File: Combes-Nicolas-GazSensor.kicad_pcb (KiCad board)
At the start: 2 copper layers, 68.6 x 53.3 mm, 8 parts, among them P1 Power, P2 Analog, P3 Digital, P4 Digital, P5 CONN_01X01, P6 CONN_01X01, P7 CONN_01X01, P8 CONN_01X01

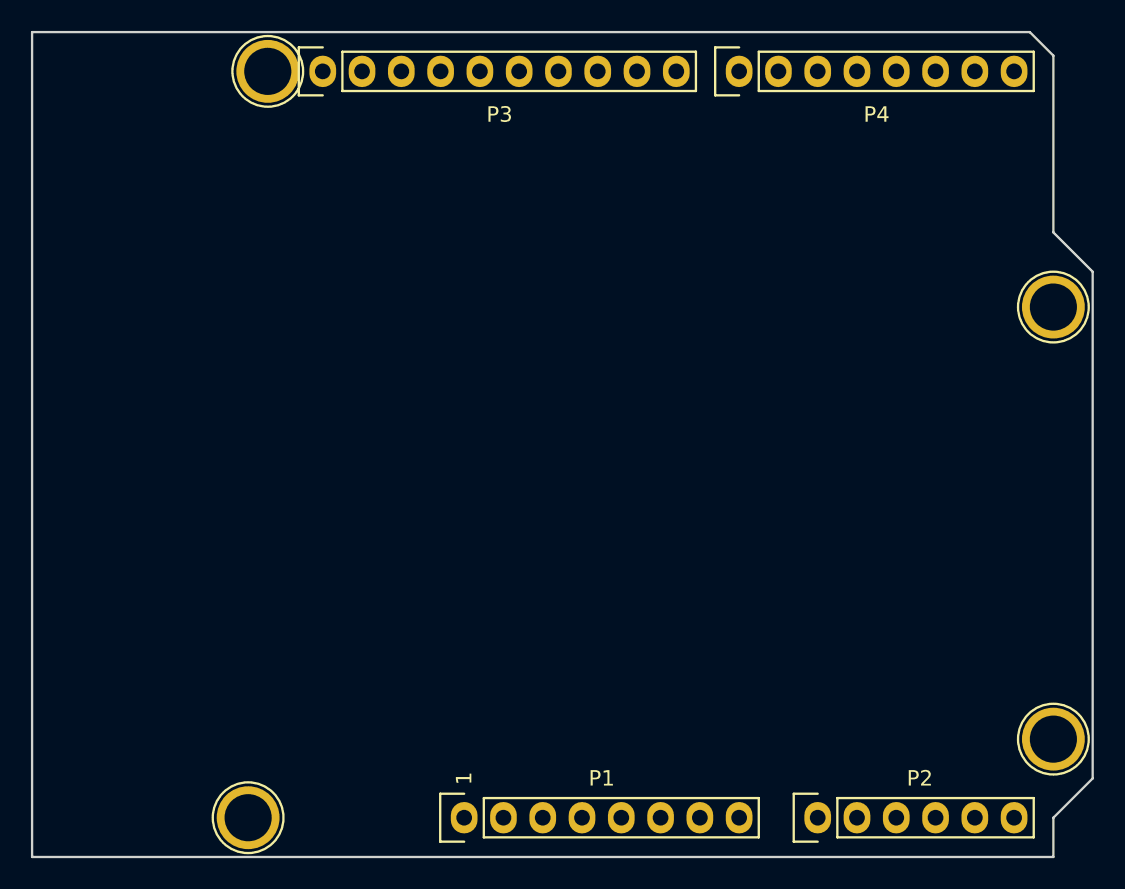
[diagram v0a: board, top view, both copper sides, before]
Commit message: Shield Capteur
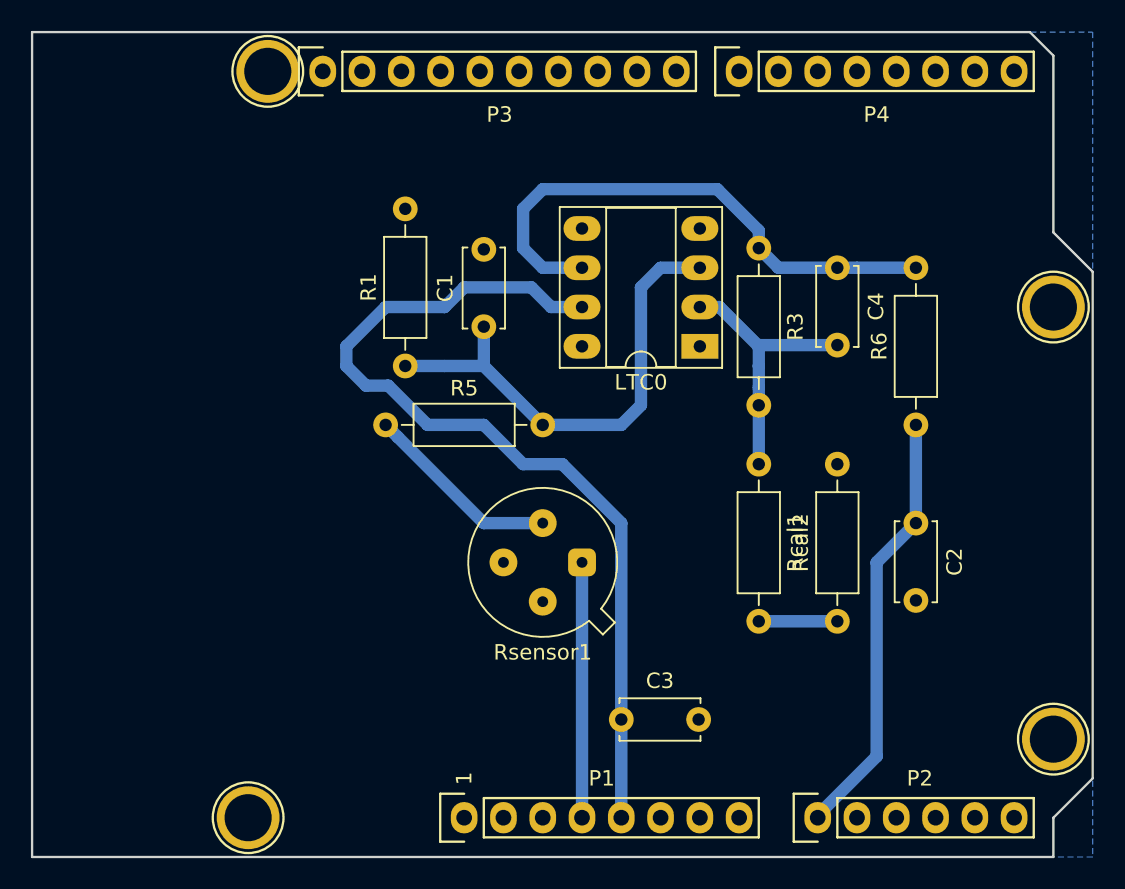
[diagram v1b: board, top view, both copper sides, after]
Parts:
- added C1: 100n, Capacitor_THT:C_Disc_D5.0mm_W2.5mm_P5.00mm, F.Cu at (140.2, 92.1)
- added C2: 100n, Capacitor_THT:C_Disc_D5.0mm_W2.5mm_P5.00mm, F.Cu at (168.1, 104.8)
- added C3: 100n, Capacitor_THT:C_Disc_D5.0mm_W2.5mm_P5.00mm, F.Cu at (149.1, 117.5)
- added C4: 1u, Capacitor_THT:C_Disc_D5.0mm_W2.5mm_P5.00mm, F.Cu at (163.1, 88.3)
- added LTC0: LTC1050, Package_DIP:DIP-8_W7.62mm_Socket_LongPads, F.Cu at (154.2, 93.3)
- added R1: 100k, Resistor_THT:R_Axial_DIN0207_L6.3mm_D2.5mm_P10.16mm_Horizontal, F.Cu at (135.1, 94.6)
- added R3: 100k, Resistor_THT:R_Axial_DIN0207_L6.3mm_D2.5mm_P10.16mm_Horizontal, F.Cu at (158.0, 87.0)
- added R5: 10k, Resistor_THT:R_Axial_DIN0207_L6.3mm_D2.5mm_P10.16mm_Horizontal, F.Cu at (133.9, 98.4)
- added R6: 1k, Resistor_THT:R_Axial_DIN0207_L6.3mm_D2.5mm_P10.16mm_Horizontal, F.Cu at (168.1, 98.4)
- added Rcal1: 1k, Resistor_THT:R_Axial_DIN0207_L6.3mm_D2.5mm_P10.16mm_Horizontal, F.Cu at (158.0, 101.0)
- added Rcal2: 220, Resistor_THT:R_Axial_DIN0207_L6.3mm_D2.5mm_P10.16mm_Horizontal, F.Cu at (163.1, 111.1)
- added Rsensor1: 10k<...<1G, MesEmpreintes:TO-5-4, F.Cu at (146.6, 107.3)
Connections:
- P1 pad 1: Net-(P1-Pad1) -> (no net)
- P1 pad 2: /IOREF -> (no net)
- P1 pad 3: /Reset -> (no net)
- P1 pad 8: /Vin -> (no net)
- P2 pad 1: /A0 -> A0
- P2 pad 2: /A1 -> (no net)
- P2 pad 3: /A2 -> (no net)
- P2 pad 4: /A3 -> (no net)
- P2 pad 5: /A4(SDA) -> (no net)
- P2 pad 6: /A5(SCL) -> (no net)
- P3 pad 1: /A5(SCL) -> (no net)
- P3 pad 10: /8 -> (no net)
- P3 pad 2: /A4(SDA) -> (no net)
- P3 pad 3: /AREF -> (no net)
- P3 pad 5: /13(SCK) -> (no net)
- P3 pad 6: /12(MISO) -> (no net)
- P3 pad 7: /11(**/MOSI) -> (no net)
- P3 pad 8: /10(**/SS) -> (no net)
- P3 pad 9: /9(**) -> (no net)
- P4 pad 1: /7 -> (no net)
- P4 pad 2: /6(**) -> (no net)
- P4 pad 3: /5(**) -> (no net)
- P4 pad 4: /4 -> (no net)
- P4 pad 5: /3(**) -> (no net)
- P4 pad 6: /2 -> (no net)
- P4 pad 7: /1(Tx) -> (no net)
- P4 pad 8: /0(Rx) -> (no net)
- P5 pad 1: Net-(P5-Pad1) -> (no net)
- P6 pad 1: Net-(P6-Pad1) -> (no net)
- P7 pad 1: Net-(P7-Pad1) -> (no net)
- P8 pad 1: Net-(P8-Pad1) -> (no net)
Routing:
- net +5V: track 0.00 -> 59.7 mm
- net Net-(C4-Pad1): track 0.00 -> 36.0 mm
- net Net-(C1-Pad1): track 0.00 -> 32.2 mm
- net A0: track 0.00 -> 28.0 mm
- net Net-(C4-Pad2): track 0.00 -> 17.6 mm
- net +3V3: track 0.00 -> 16.5 mm
- net Net-(R5-Pad1): track 0.00 -> 12.8 mm
- net Net-(Rcal1-Pad2): track 0.00 -> 5.08 mm
- added copper zone on B.Cu, net GND
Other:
- net class Default: clearance 0.2 -> 0.4; trace_width 0.25 -> 0.8; via_dia 0.6 -> 1.6; via_drill 0.4 -> 0.8
- rule trace_clearance: 0.2 -> 0.4
